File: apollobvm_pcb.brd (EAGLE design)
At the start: 98 x 60 mm, 25 parts

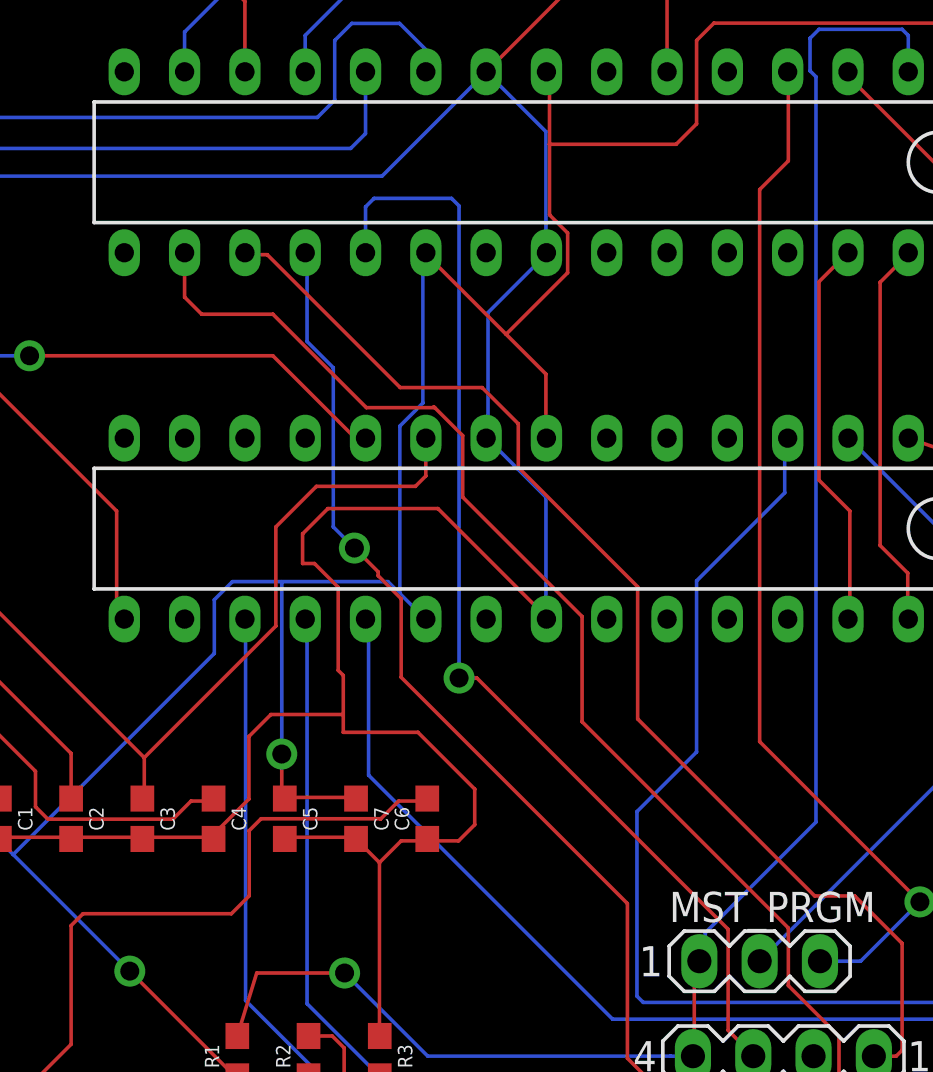
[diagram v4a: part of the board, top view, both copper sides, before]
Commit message: Fixed close traces
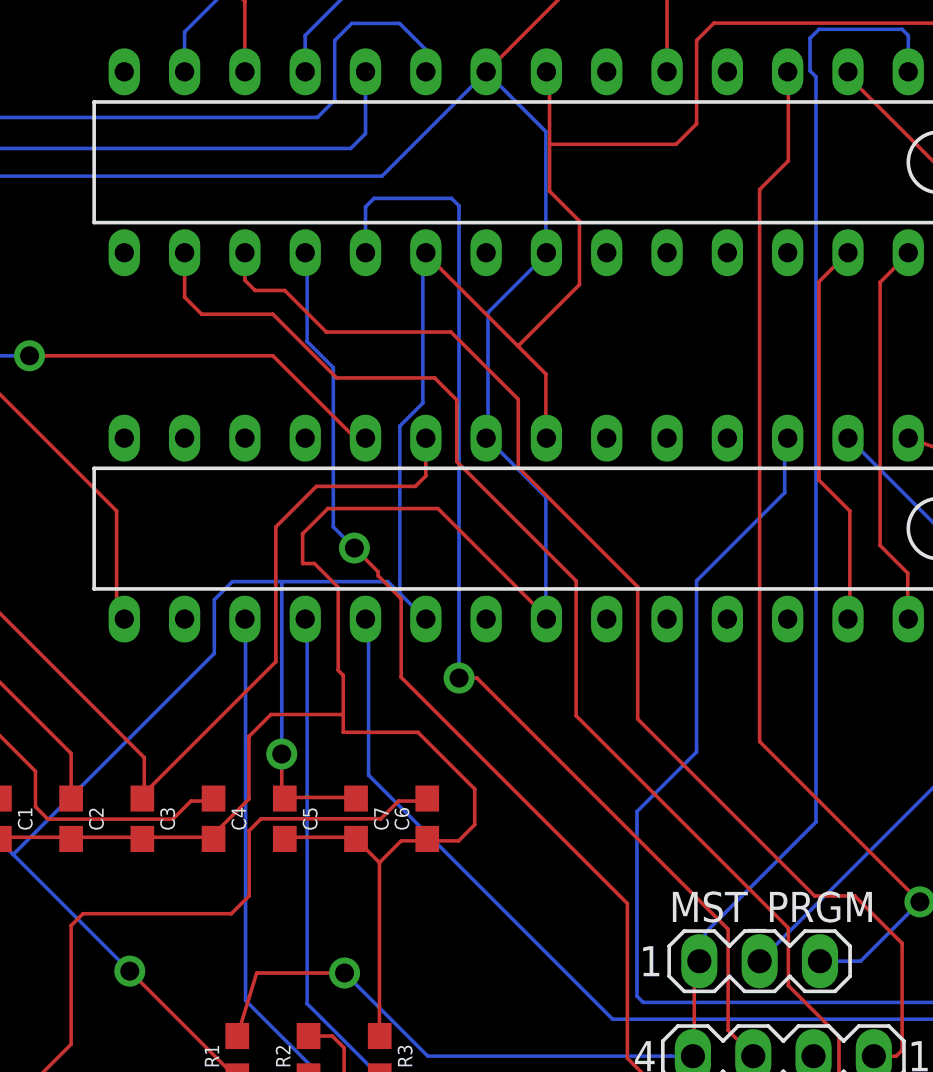
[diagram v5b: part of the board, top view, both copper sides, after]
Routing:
- net N$3: track 43.8 -> 45.3 mm
- net N$18: track 49.9 -> 51.1 mm
- net +5V: track 170.0 -> 170.7 mm
- net N$14: track 104.3 -> 104.9 mm
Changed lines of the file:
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@@
 <wire x1="89.916" y1="44.6532" x2="90" y2="44.54" width="0.1524" layer="1"/>
 <wire x1="56.9976" y1="36.7284" x2="56.9976" y2="34.1376" width="0.1524" layer="1"/>
-<wire x1="51.9684" y1="41.7576" x2="55.3212" y2="38.4048" width="0.1524" layer="1"/>
-<wire x1="55.3212" y1="38.4048" x2="56.9976" y2="36.7284" width="0.1524" layer="1"/>
+<wire x1="51.9684" y1="41.7576" x2="55.8212" y2="37.9048" width="0.1524" layer="1"/>
+<wire x1="55.8212" y1="37.9048" x2="56.9976" y2="36.7284" width="0.1524" layer="1"/>
 <wire x1="56.9976" y1="34.1376" x2="57.02" y2="34.03" width="0.1524" layer="1"/>
 <wire x1="51.9684" y1="41.7576" x2="51.94" y2="41.84" width="0.1524" layer="1"/>
-<wire x1="57.15" y1="43.434" x2="57.15" y2="46.4084" width="0.1524" layer="1"/>
+<wire x1="57.15" y1="44.434" x2="57.15" y2="46.4084" width="0.1524" layer="1"/>
 <wire x1="57.15" y1="46.4084" x2="57.15" y2="49.3776" width="0.1524" layer="1"/>
-<wire x1="57.912" y1="42.672" x2="57.15" y2="43.434" width="0.1524" layer="1"/>
-<wire x1="57.912" y1="40.9956" x2="57.912" y2="42.672" width="0.1524" layer="1"/>
-<wire x1="55.3212" y1="38.4048" x2="57.912" y2="40.9956" width="0.1524" layer="1"/>
+<wire x1="58.412" y1="43.172" x2="57.15" y2="44.434" width="0.1524" layer="1"/>
+<wire x1="58.412" y1="40.4956" x2="58.412" y2="43.172" width="0.1524" layer="1"/>
+<wire x1="55.8212" y1="37.9048" x2="58.412" y2="40.4956" width="0.1524" layer="1"/>
 <wire x1="57.15" y1="49.3776" x2="57.02" y2="49.46" width="0.1524" layer="1"/>
 <wire x1="48.9204" y1="18.8976" x2="46.0248" y2="18.8976" width="0.1524" layer="1"/>
@@
 <contactref element="SLAVE" pad="9"/>
 <contactref element="Q2" pad="1"/>
-<wire x1="40.0812" y1="20.574" x2="40.0812" y2="18.8976" width="0.1524" layer="1"/>
-<wire x1="45.6224" y1="26.1152" x2="40.0812" y2="20.574" width="0.1524" layer="1"/>
-<wire x1="45.6224" y1="26.1152" x2="45.6224" y2="30.2916" width="0.1524" layer="1"/>
+<wire x1="40.0812" y1="20.574" x2="40.0812" y2="19.074" width="0.1524" layer="1"/>
+<wire x1="40.0812" y1="19.074" x2="40.0812" y2="18.8976" width="0.1524" layer="1"/>
+<wire x1="45.6224" y1="24.6152" x2="40.0812" y2="19.074" width="0.1524" layer="1"/>
+<wire x1="45.6224" y1="24.6152" x2="45.6224" y2="30.2916" width="0.1524" layer="1"/>
 <wire x1="40.0812" y1="18.8976" x2="40" y2="18.85" width="0.1524" layer="1"/>
 <wire x1="30.3276" y1="30.3276" x2="23.0124" y2="30.3276" width="0.1524" layer="1"/>
@@
 <wire x1="51.9016" y1="5.2484" x2="50" y2="7.15" width="0.1524" layer="1"/>
 <wire x1="89.916" y1="22.7076" x2="90" y2="22.73" width="0.1524" layer="1"/>
-<wire x1="53.4924" y1="34.1376" x2="52.315" y2="35.315" width="0.1524" layer="1"/>
-<wire x1="52.315" y1="35.315" x2="52.2732" y2="35.3568" width="0.1524" layer="1"/>
-<wire x1="53.4924" y1="31.5468" x2="53.4924" y2="34.1376" width="0.1524" layer="1"/>
-<wire x1="58.5216" y1="26.5176" x2="53.4924" y2="31.5468" width="0.1524" layer="1"/>
-<wire x1="58.5216" y1="22.086" x2="58.5216" y2="26.5176" width="0.1524" layer="1"/>
-<wire x1="67.2084" y1="13.3992" x2="58.5216" y2="22.086" width="0.1524" layer="1"/>
+<wire x1="53.2424" y1="35.6376" x2="52.315" y2="36.565" width="0.1524" layer="1"/>
+<wire x1="53.2424" y1="33.0468" x2="53.2424" y2="35.6376" width="0.1524" layer="1"/>
+<wire x1="58.2716" y1="28.0176" x2="53.2424" y2="33.0468" width="0.1524" layer="1"/>
+<wire x1="58.2716" y1="22.336" x2="58.2716" y2="28.0176" width="0.1524" layer="1"/>
+<wire x1="67.2084" y1="13.3992" x2="58.2716" y2="22.336" width="0.1524" layer="1"/>
 <wire x1="67.2084" y1="10.9728" x2="67.2084" y2="13.3992" width="0.1524" layer="1"/>
 <wire x1="69.342" y1="8.8392" x2="67.2084" y2="10.9728" width="0.1524" layer="1"/>
@@
 <wire x1="45.5" y1="39.25" x2="42.5" y2="39.25" width="0.1524" layer="1"/>
 <wire x1="41.78" y1="39.97" x2="42.5" y2="39.25" width="0.1524" layer="1"/>
-<wire x1="52.315" y1="35.315" x2="49.435" y2="35.315" width="0.1524" layer="1"/>
-<wire x1="49.435" y1="35.315" x2="45.5" y2="39.25" width="0.1524" layer="1"/>
+<wire x1="52.315" y1="36.565" x2="48.185" y2="36.565" width="0.1524" layer="1"/>
+<wire x1="48.185" y1="36.565" x2="45.5" y2="39.25" width="0.1524" layer="1"/>
 </signal>
 <signal name="N$15">
@@
 <contactref element="MST_BOOT" pad="1"/>
 <contactref element="MASTER" pad="17"/>
-<wire x1="45.2628" y1="41.7576" x2="44.3484" y2="41.7576" width="0.1524" layer="1"/>
-<wire x1="50.8588" y1="36.1616" x2="45.2628" y2="41.7576" width="0.1524" layer="1"/>
-<wire x1="54.3092" y1="36.1616" x2="50.8588" y2="36.1616" width="0.1524" layer="1"/>
-<wire x1="55.8332" y1="34.6376" x2="54.3092" y2="36.1616" width="0.1524" layer="1"/>
-<wire x1="55.8332" y1="32.7968" x2="55.8332" y2="34.6376" width="0.1524" layer="1"/>
 <wire x1="60.8624" y1="27.7676" x2="55.8332" y2="32.7968" width="0.1524" layer="1"/>
 <wire x1="60.8624" y1="27.7676" x2="60.8624" y2="22.2024" width="0.1524" layer="1"/>
-<wire x1="44.3484" y1="41.7576" x2="44.32" y2="41.84" width="0.1524" layer="1"/>
 <wire x1="68.3148" y1="14.75" x2="70" y2="14.75" width="0.1524" layer="1"/>
 <wire x1="70" y1="14.75" x2="72" y2="12.75" width="0.1524" layer="1"/>
@@
 <wire x1="71.75" y1="8" x2="70.81" y2="8" width="0.1524" layer="1"/>
 <wire x1="60.8624" y1="22.2024" x2="68.3148" y2="14.75" width="0.1524" layer="1"/>
+<wire x1="46" y1="40.25" x2="44.75" y2="40.25" width="0.1524" layer="1"/>
+<wire x1="44.75" y1="40.25" x2="44.32" y2="40.68" width="0.1524" layer="1"/>
+<wire x1="44.32" y1="40.68" x2="44.32" y2="41.84" width="0.1524" layer="1"/>
+<wire x1="55.8332" y1="32.7968" x2="55.8332" y2="35.6668" width="0.1524" layer="1"/>
+<wire x1="55.8332" y1="35.6668" x2="53" y2="38.5" width="0.1524" layer="1"/>
+<wire x1="53" y1="38.5" x2="47.75" y2="38.5" width="0.1524" layer="1"/>
+<wire x1="47.75" y1="38.5" x2="46" y2="40.25" width="0.1524" layer="1"/>
 </signal>
 <signal name="N$19">
